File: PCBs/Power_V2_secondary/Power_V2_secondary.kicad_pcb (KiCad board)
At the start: 2 copper layers, 44.9 x 99.8 mm, 16 parts, among them IC7 ACS712ELCTR-20A-T, J1 PCIE-164-02-F-D-TH-TR, J2 Conn_01x10, J8 Conn_01x02, U1 01530007Z

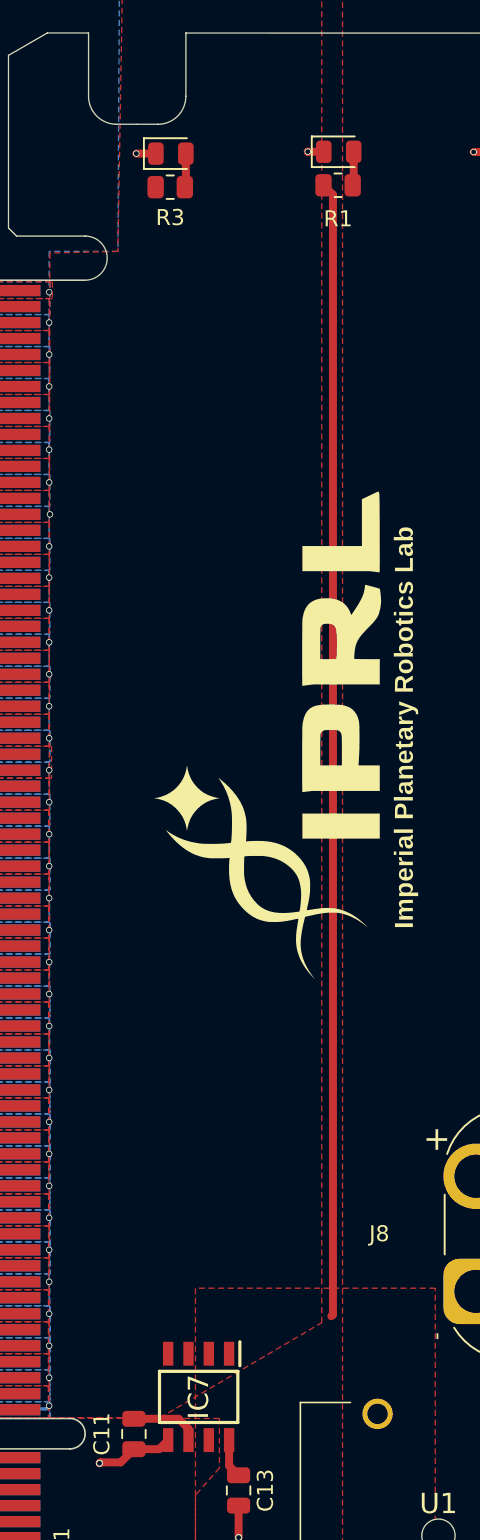
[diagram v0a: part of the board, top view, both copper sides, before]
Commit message: 12 to 5V regulator added
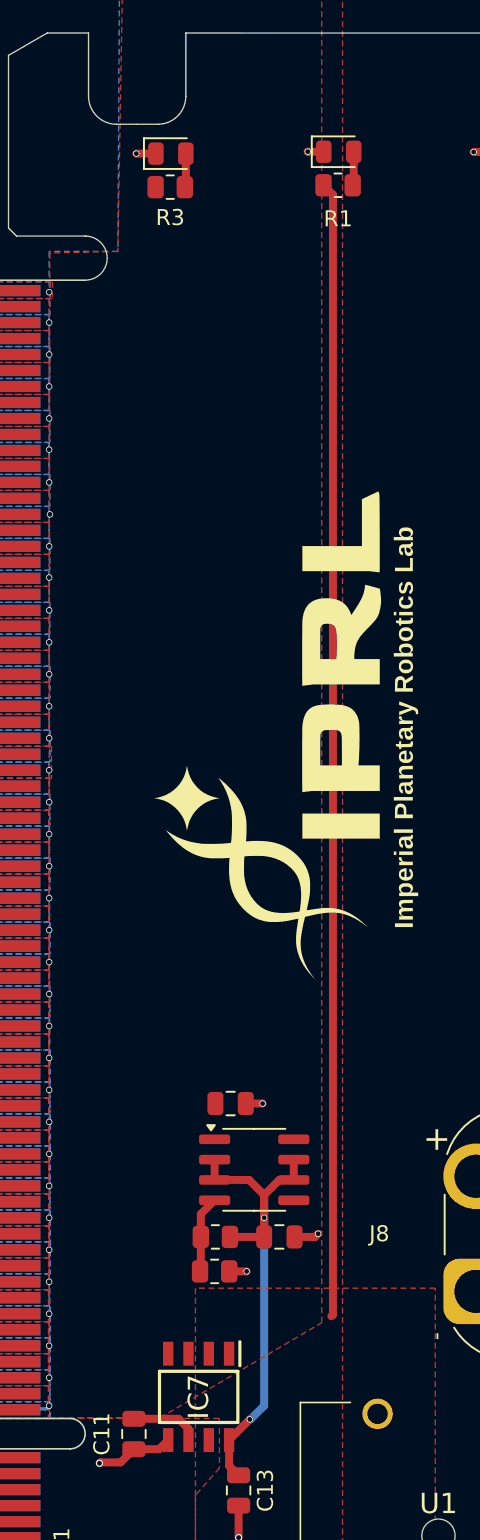
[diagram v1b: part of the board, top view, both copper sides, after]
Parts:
- added C23: 100n, Capacitor_SMD:C_0805_2012Metric, F.Cu at (104.6, 92.8)
- added C24: 1u, Capacitor_SMD:C_0805_2012Metric, F.Cu at (107.6, 101.1)
- added R25: 720, Resistor_SMD:R_0805_2012Metric, F.Cu at (103.6, 103.3)
- added R26: 240, Resistor_SMD:R_0805_2012Metric, F.Cu at (103.6, 101.1)
- added U10: LM317L_SO8, Package_SO:SOIC-8_3.9x4.9mm_P1.27mm, F.Cu at (106.1, 96.9)
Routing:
- net +5V: track 2.45 -> 32.9 mm, vias 0 -> 2
- net Net-(U10-ADJ): track 0.00 -> 4.83 mm
- net GND: track 10.6 -> 14.2 mm, vias 23 -> 26
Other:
- outline, holes or cut-outs redrawn

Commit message: arm, drive and power modifications
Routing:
- net +5V: track 32.9 -> 34.1 mm
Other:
- board text added: "Designed by James King"
- board text added: "POWER BOARD: SECONDARY V2"
- board text removed: "POWER BOARD: SECONDARY"
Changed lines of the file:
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@@
 			(drillshape 0)
 			(scaleselection 1)
-			(outputdirectory "./")
+			(outputdirectory "Outputs/")
 		)
 	)
@@
 		)
 	)
-	(gr_text "POWER BOARD:\nSECONDARY"
+	(gr_text "Designed by James King"
+		(at 115.568328 77.250172 90)
+		(layer "B.SilkS" knockout)
+		(effects
+			(font
+				(size 1 1)
+				(thickness 0.15)
+			)
+			(justify left bottom mirror)
+		)
+	)
+	(gr_text "POWER BOARD:\nSECONDARY V2"
 		(at 114.1 62.3 90)
 		(layer "B.SilkS" knockout)
@@
 	)
 	(segment
+		(start 106.6975 98.52125)
+		(end 106.6975 103.5)
+		(width 0.5)
+		(layer "F.Cu")
+		(net 3)
+	)
+	(segment
 		(start 108.55 97.57875)
 		(end 107.64 97.57875)
@@
 	(segment
 		(start 106.6975 101.14375)
-		(end 106.6975 99.94375)
+		(end 106.6975 103.5)
 		(width 0.5)
 		(layer "F.Cu")
@@
 		(net 3)
 	)
-	(segment
-		(start 106.6975 98.52125)
-		(end 106.6975 99.94375)
-		(width 0.5)
-		(layer "F.Cu")
-		(net 3)
-	)
 	(via
-		(at 106.6975 99.94375)
+		(at 106.6975 103.5)
 		(size 0.4)
 		(drill 0.3)
@@
 	(segment
 		(start 106.6975 111.7025)
-		(end 106.6975 99.94375)
+		(end 105.845 112.555)
 		(width 0.5)
 		(layer "B.Cu")
@@
 	)
 	(segment
-		(start 105.845 112.555)
+		(start 106.6975 103.5)
 		(end 106.6975 111.7025)
 		(width 0.5)
@@
 	)
 	(segment
-		(start 105.8 112.555)
-		(end 105.845 112.555)
+		(start 105.845 112.555)
+		(end 105.8 112.555)
 		(width 0.5)
 		(layer "B.Cu")
@@
 		(polygon
 			(pts
-				(xy 102.475 95.54375) (xy 101.675 95.54375) (xy 101.675 96.24375) (xy 102.475 96.24375)
+				(xy 102.475 95.54375) (xy 102.075 95.54375) (xy 102.075 96.24375) (xy 102.475 96.24375)
 			)
 		)
